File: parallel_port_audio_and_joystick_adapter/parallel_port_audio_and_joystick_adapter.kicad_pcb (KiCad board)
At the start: 2 copper layers, 36.8 x 36.8 mm, 6 parts, among them J1 DB25_Male, J2 DB9_Male, J3 AudioJack2

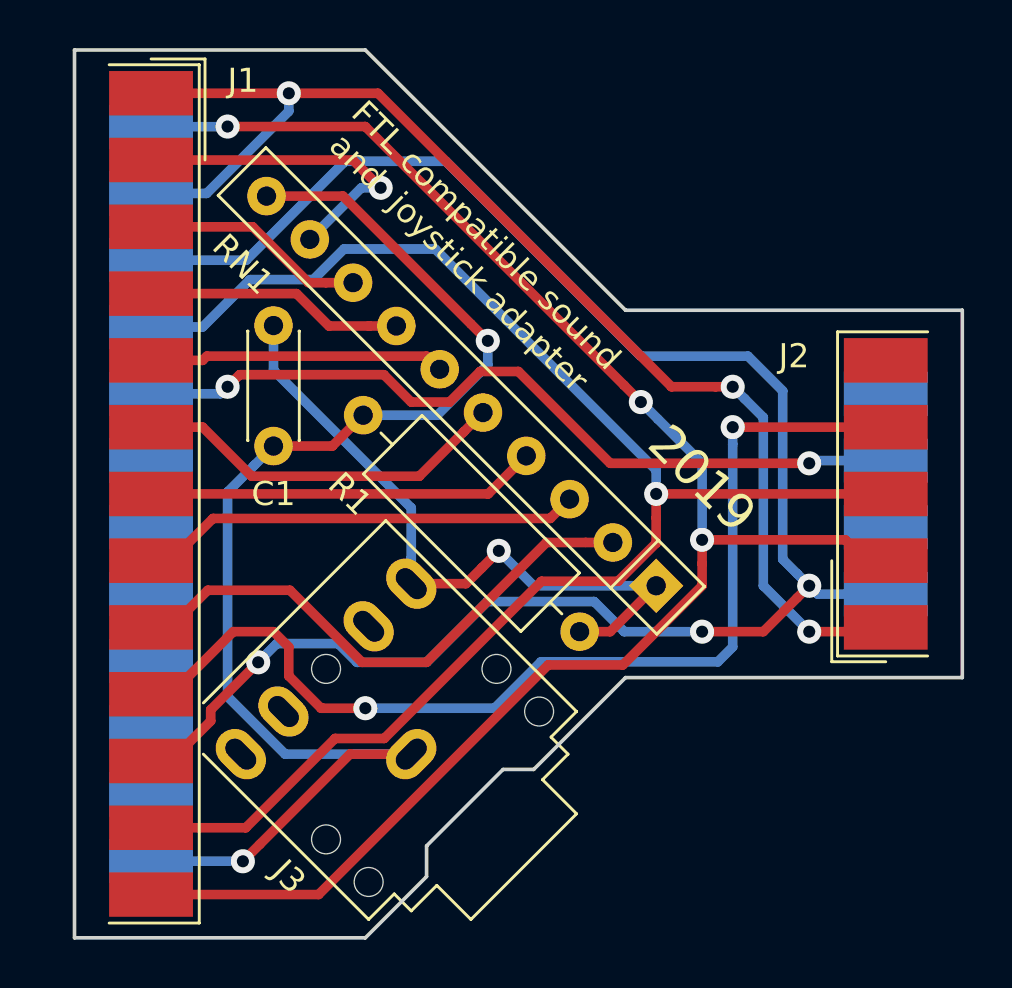
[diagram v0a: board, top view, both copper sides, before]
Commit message: add resistors in series to prevent short circuit
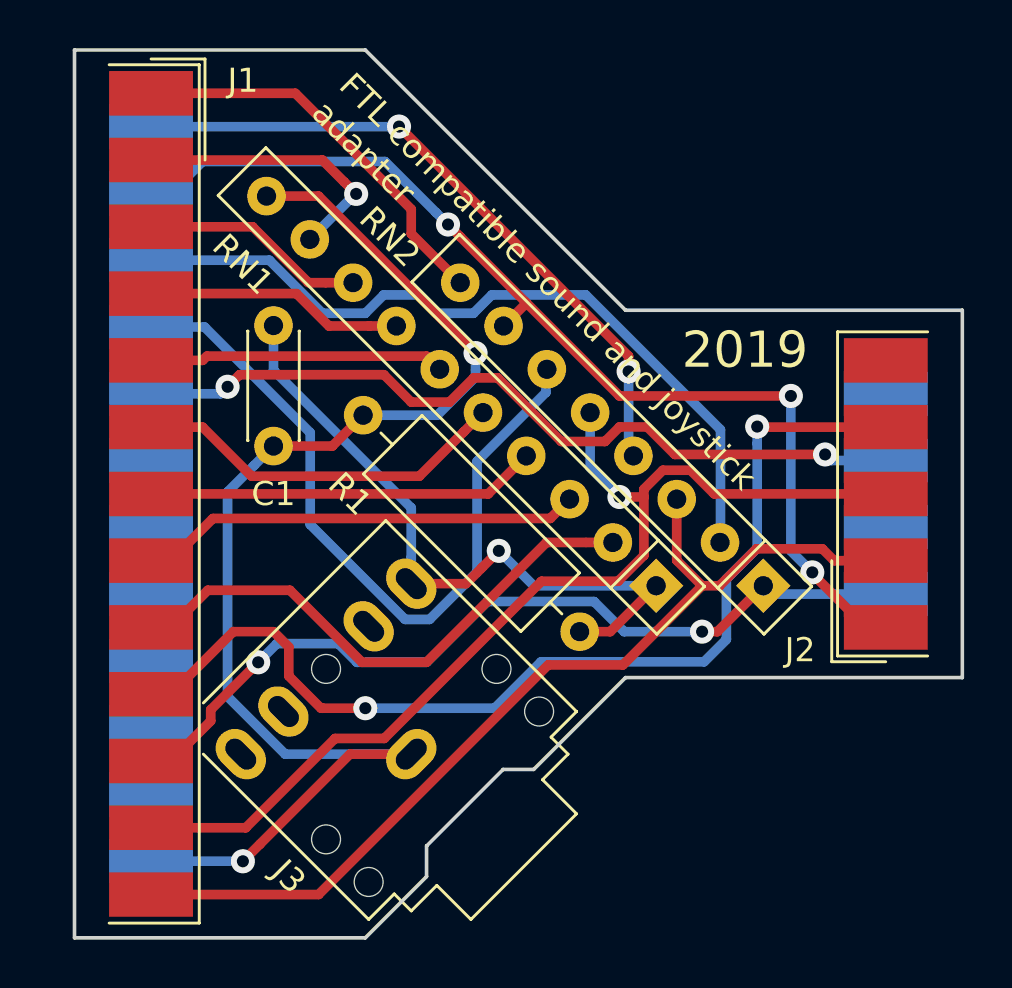
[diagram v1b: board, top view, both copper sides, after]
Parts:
- added RN2: R_Pack04_SIP, Resistor_THT:R_Array_SIP8, F.Cu at (109.9, 95.2)
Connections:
- J1 pad 14: Net-(J1-Pad13) -> Net-(J1-Pad14)
- J1 pad 15: Net-(J1-Pad1) -> Net-(J1-Pad15)
- J1 pad 16: Net-(J1-Pad11) -> Net-(J1-Pad16)
- J1 pad 17: Net-(J1-Pad12) -> Net-(J1-Pad17)
- J2 pad 1: Net-(J1-Pad1) -> Net-(J1-Pad15)
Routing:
- net Net-(J1-Pad15): track 0.00 -> 44.2 mm, vias 0 -> 3
- net Net-(J1-Pad11): track 76.0 -> 35.6 mm, vias 3 -> 2
- net Net-(J1-Pad1): track 51.8 -> 16.7 mm, vias 3 -> 0
- net Net-(J1-Pad16): track 0.00 -> 32.5 mm
- net Net-(J1-Pad17): track 0.00 -> 31.2 mm
- net Net-(J1-Pad13): track 69.9 -> 40.7 mm, vias 3 -> 0
- net Net-(J1-Pad14): track 0.00 -> 27.9 mm, vias 0 -> 2
- net Net-(J1-Pad12): track 64.5 -> 43.7 mm
- net Net-(J1-Pad2): track 13.8 -> 11.8 mm
- net Net-(C1-Pad2): track 55.4 -> 54.4 mm
- net Net-(J1-Pad10): track 43.7 -> 42.9 mm

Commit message: move traces further away from holes
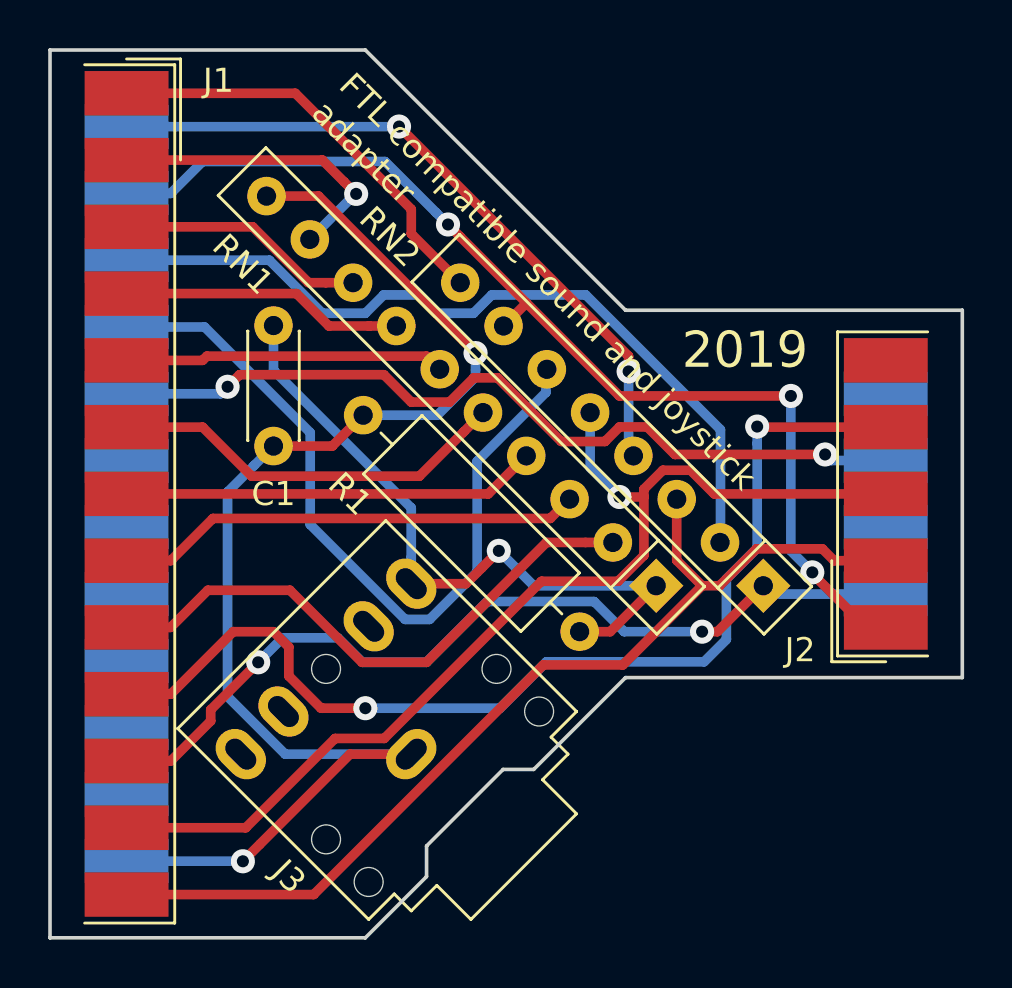
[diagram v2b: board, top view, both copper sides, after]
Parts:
- moved J1 1.02 mm to (83.4, 91.4)
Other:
- board size 36.8 x 36.8 mm -> 37.8 x 36.8 mm
